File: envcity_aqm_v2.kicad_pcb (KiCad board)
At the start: 2 copper layers, 100 x 100 mm, 127 parts, among them IC1 DS1307ZN+, IC2 DMMT5401-7F, IC3 DMMT5401-7F, IC4 DMMT5401-7-F, IC6 ESP32-S2-SOLO-N4R2, J1 USB_B_Micro, J12 Conn_01x06_Male, J13 Conn_01x06_Male, J14 Conn_01x08_Pin, J15 Conn_01x02_Male, J16 Conn_01x02_Male, J2 Screw_Terminal_01x02, J3 Screw_Terminal_01x02, J6 Conn_01x04_Male, J7 Conn_01x06_Pin, J8 503398-1892, Q1 DMG2301L / DMP2045U, Q2 DMG2301L / DMP2045U, Q3 DMG2301L, Q4 DMG2301L, Q5 DMG2301L / DMP2045U, Q6 DMG2301L, Q7 DMN10H220L, Q8 DMN10H220L, SW1 RESET, SW2 BOOT, U1 TP4056, U10 RFM95W-915S2, U11 ADS1115IDGS, U2 USBLC6-2SC6, U3 MT3608, U5 LM2596S-5, U6 AP2112K-3.3, U7 DHT11, U8 AP2112K-3.3, U9 74HC4067DB, Y2 AB26TRB

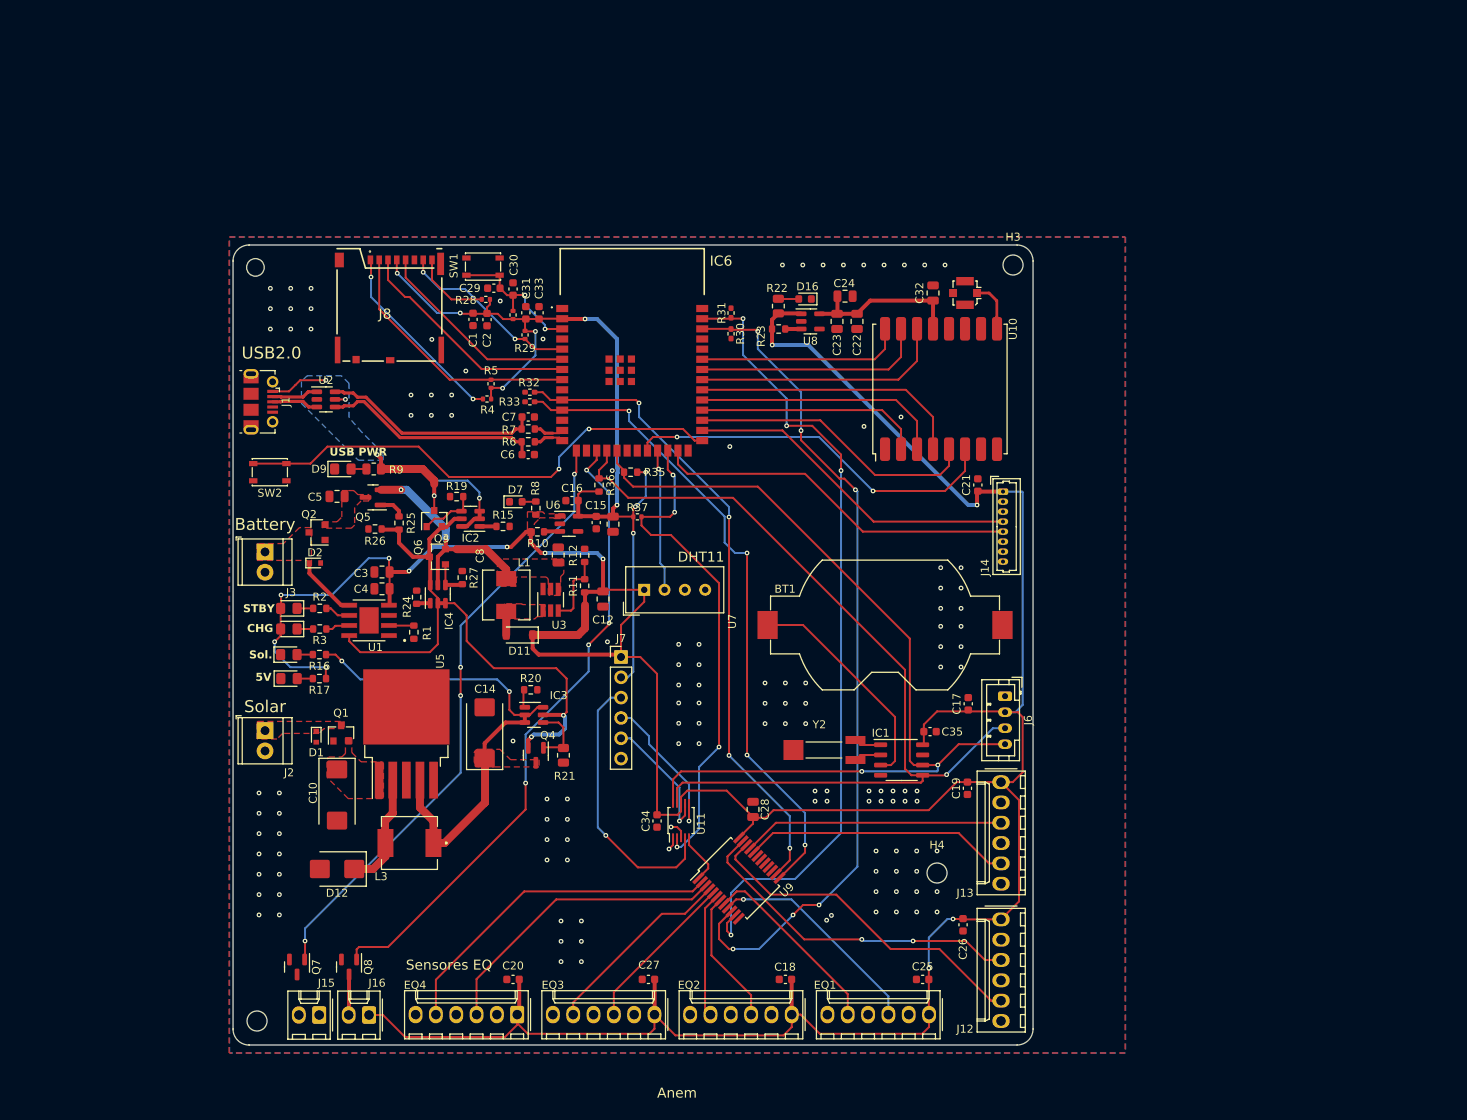
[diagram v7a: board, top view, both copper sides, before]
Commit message: board ok. Add tps54202
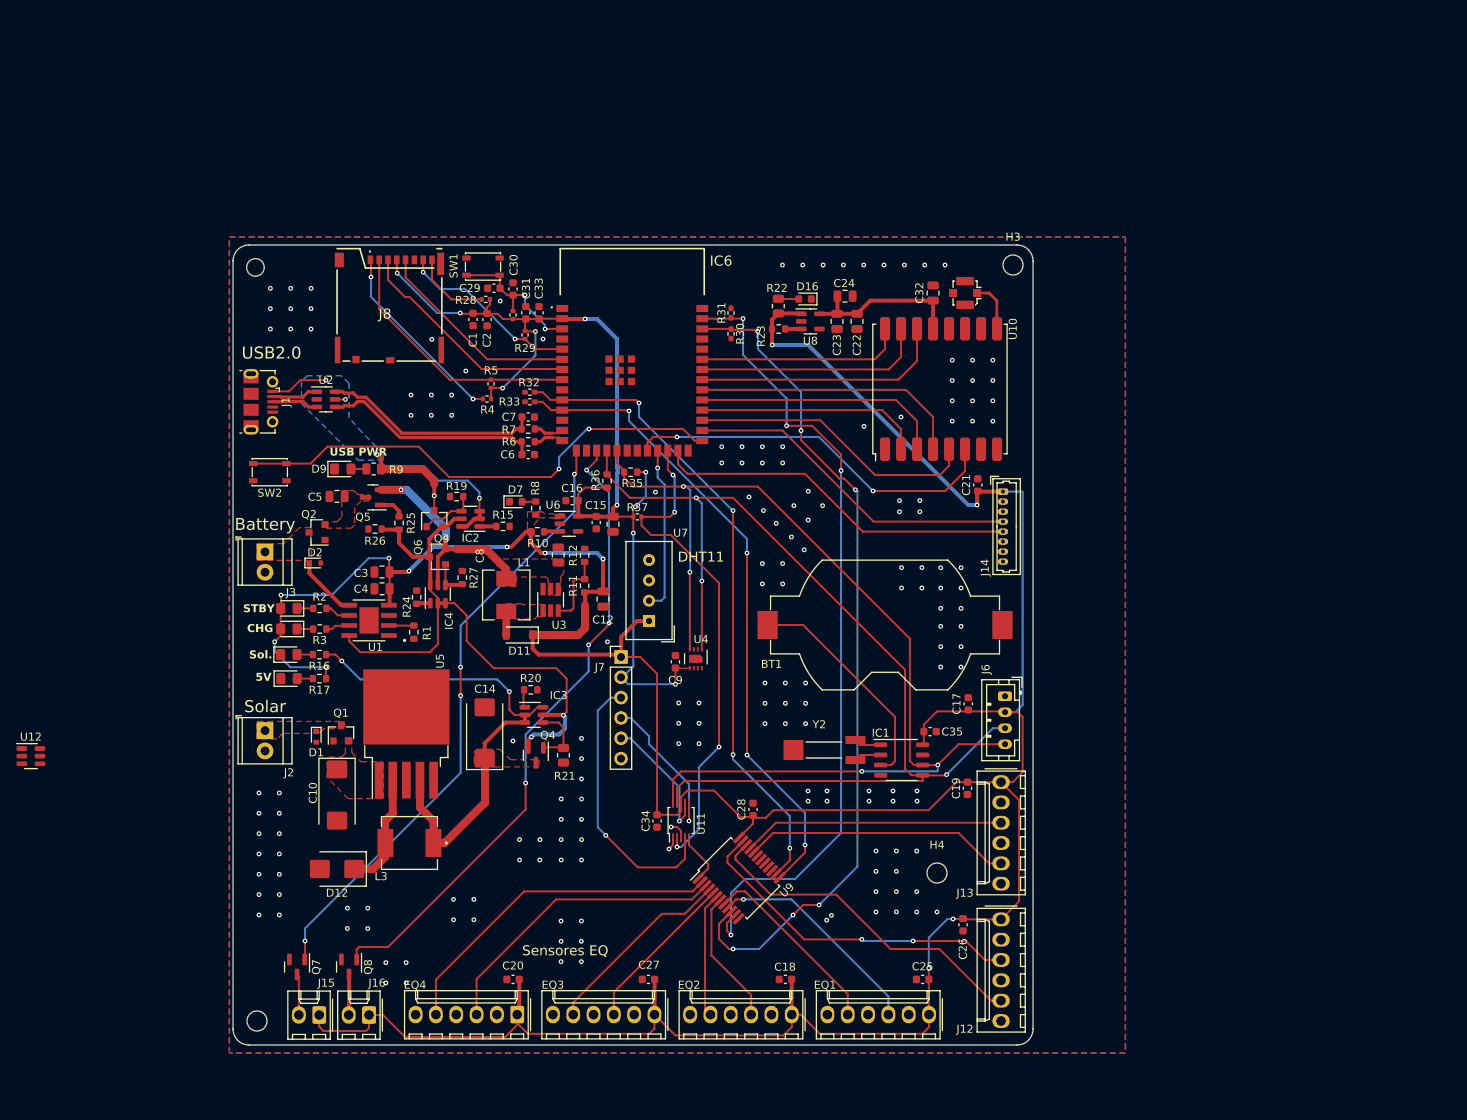
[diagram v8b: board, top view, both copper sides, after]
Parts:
- added C9: 100nF, Capacitor_SMD:C_0603_1608Metric, F.Cu at (166.3, 112.1)
- added U12: TPS54202DDC, Package_TO_SOT_SMD:SOT-23-6, F.Cu at (85.7, 123.9)
- added U4: SHT30-DIS, Sensor_Humidity:Sensirion_DFN-8-1EP_2.5x2.5mm_P0.5mm_EP1.1x1.7mm, F.Cu at (168.8, 111.7)
- C28: footprint Capacitor_SMD:C_0805_2012Metric -> Capacitor_SMD:C_0603_1608Metric
- moved U7 3.95 mm to (163.0, 107.0), turned to 180 degrees
- moved R36 1.12 mm to (157.8, 89.5)
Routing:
- net /SCL: track 113.3 -> 134.3 mm, vias 2 -> 4
- net /SDA: track 113.4 -> 131.0 mm, vias 1 -> 3
- net +3V3: track 111.7 -> 123.5 mm, vias 9 -> 10
- net Net-(J15-Pin_2): track 0.00 -> 5.16 mm
- net /DHT_PIN: track 17.8 -> 20.8 mm
- net +5V: track 424.5 -> 426.7 mm
- net /S3: track 82.0 -> 81.1 mm
- net GND: track 3.91 -> 4.27 mm, vias 128 -> 174
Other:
- board text removed: "Anem"
